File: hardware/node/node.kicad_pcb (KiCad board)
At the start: 4 copper layers, 50 x 50 mm, 71 parts, among them J1 BOOT0_Jumper, J2 FTDI, J3 SMA Female, J4 2 x AA, J5 SWD, Q1 Si2323DDS, SW1 TVCM04N016BB, U1 RFM69HW, U2 SHTC3, U3 AT25DF512C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

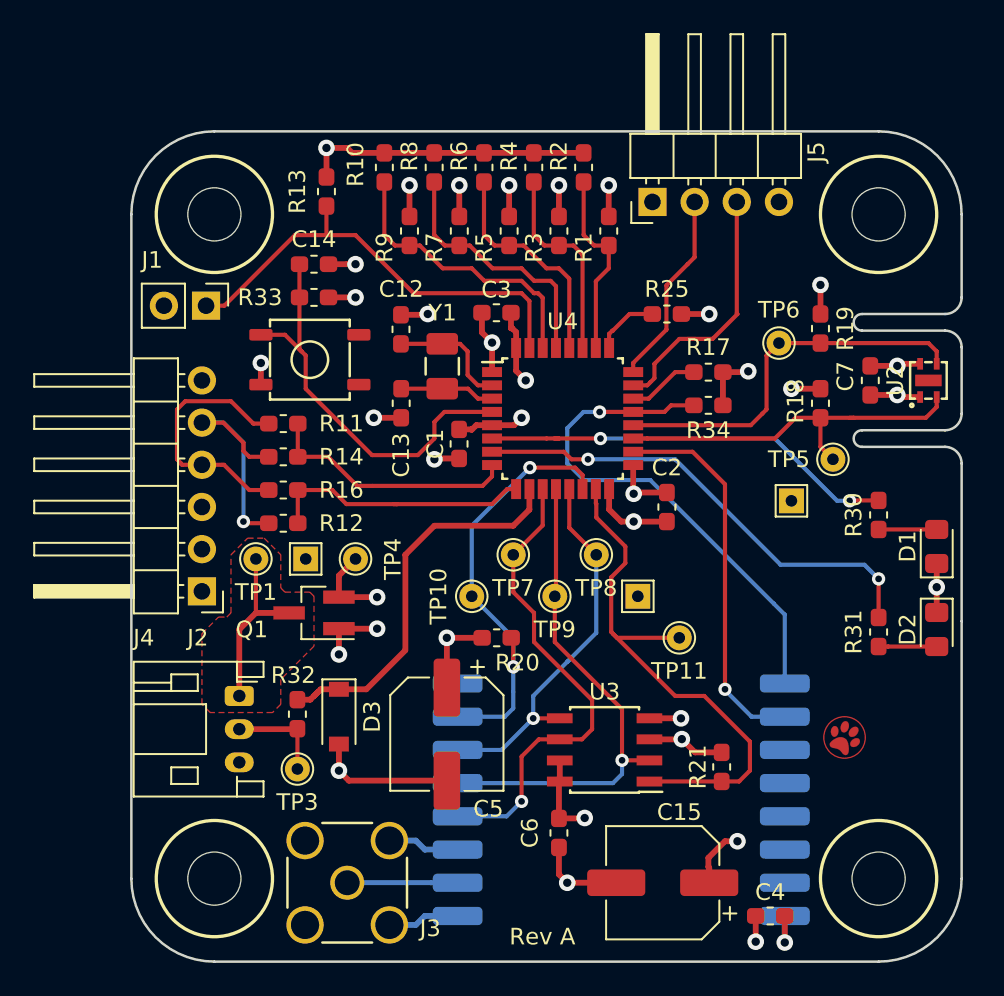
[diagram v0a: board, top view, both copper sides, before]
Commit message: Moved mounting holes. Slightly narrower PCB
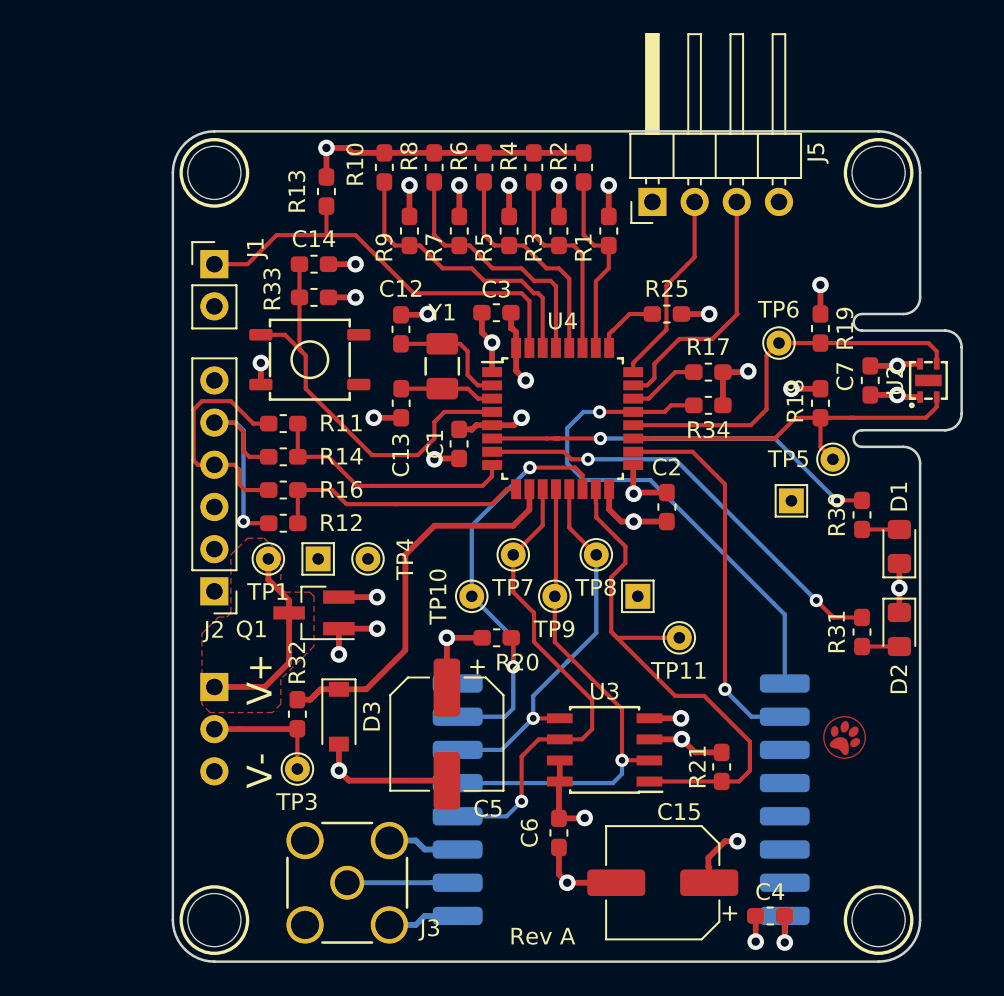
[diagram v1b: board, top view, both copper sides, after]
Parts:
- J2: footprint Connector_PinHeader_2.54mm:PinHeader_1x06_P2.54mm_Horizontal -> Connector_PinHeader_2.54mm:PinHeader_1x06_P2.54mm_Vertical
- J4: footprint Connector_JST:JST_PH_S3B-PH-K_1x03_P2.00mm_Horizontal -> Connector_PinHeader_2.54mm:PinHeader_1x03_P2.54mm_Vertical; moved to B.Cu
- moved J1 2.55 mm to (60.0, 58.0), turned to 0 degrees
- moved H1 2.50 mm to (100.0, 97.5)
- moved H2 2.50 mm to (60.0, 97.5)
- moved H3 2.50 mm to (60.0, 52.5)
- moved H4 2.50 mm to (100.0, 52.5)
- moved D1 2.25 mm to (101.2, 75.0)
- moved D2 2.25 mm to (101.2, 80.0)
- moved J4 1.59 mm to (60.0, 83.5), turned to 180 degrees
- moved R30 1.00 mm to (99.0, 73.1)
- moved R31 1.00 mm to (99.0, 80.2)
- moved J2 0.75 mm to (60.0, 77.7)
- moved TP1 0.75 mm to (63.2, 75.8)
- moved TP2 0.75 mm to (66.2, 75.8)
- moved TP4 0.75 mm to (69.2, 75.8)
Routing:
- net GND: track 288.3 -> 273.5 mm
- net VCC: track 211.7 -> 208.2 mm
- net /LEDG: track 28.8 -> 26.4 mm
- net /BOOT0: track 27.5 -> 25.9 mm
- net /V_BAT_MID: track 5.94 -> 7.44 mm
- net /FTDI_TX: track 15.6 -> 14.3 mm
- net Net-(D2-Pad2): track 3.50 -> 2.25 mm
- net Net-(D1-Pad2): track 3.50 -> 2.25 mm
- net /V_BAT: track 10.7 -> 11.9 mm
- net /LEDR: track 25.1 -> 24.1 mm
- net /FTDI_RX: track 14.5 -> 13.8 mm
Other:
- board size 50 x 50 mm -> 47.5 x 50 mm
- board text added: "Olof Ohlsson Sax 2019-06-03"
- board text removed: "Olof Ohlsson Sax 2019-05-28"

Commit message: Move power connector to other side
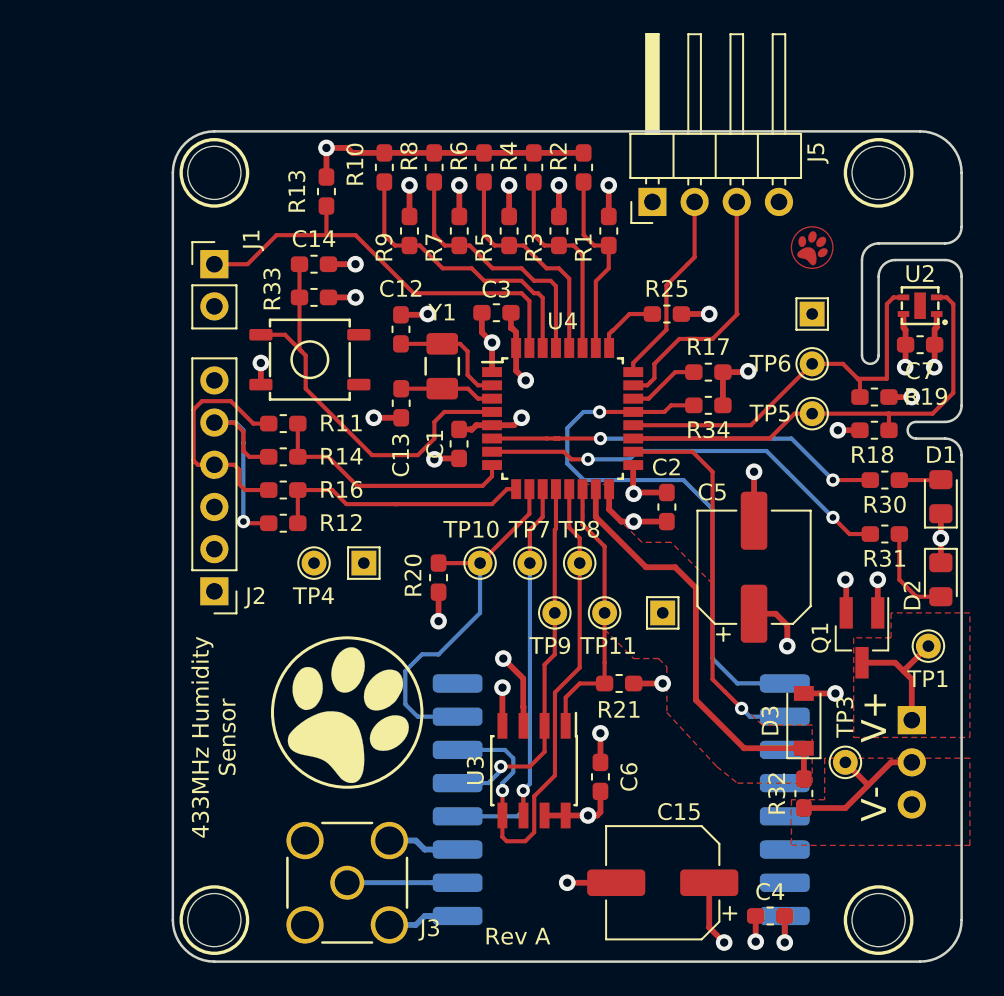
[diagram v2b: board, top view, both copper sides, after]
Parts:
- added G***: LOGO, humidity:paw-large-screen-circ, F.Cu at (68.0, 85.0)
- moved J4 42.0 mm to (102.0, 85.5)
- moved TP1 40.1 mm to (103.0, 81.0)
- moved Q1 33.0 mm to (99.0, 80.5), turned to 270 degrees
- moved TP3 33.0 mm to (98.0, 88.0)
- moved R32 30.9 mm to (95.5, 89.9)
- moved G*** 29.6 mm to (96.0, 57.0)
- moved D3 28.0 mm to (95.5, 85.5), turned to 90 degrees
- moved C5 21.1 mm to (92.5, 76.2), turned to 90 degrees
- moved TP13 11.3 mm to (96.0, 61.0)
- moved R21 7.96 mm to (84.4, 83.2), turned to 0 degrees
- moved R31 6.06 mm to (100.4, 74.2), turned to 180 degrees
- moved R19 5.25 mm to (99.8, 66.0), turned to 0 degrees
- moved R20 5.04 mm to (73.5, 76.9), turned to 270 degrees
- moved TP11 4.74 mm to (83.5, 79.0)
- moved U2 4.53 mm to (102.5, 60.5), turned to 180 degrees
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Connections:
- U4 pad 10: /BAT_MID -> /CS_RFM69
- U4 pad 14: /CS_RFM69 -> /CS_FLASH
- U4 pad 15: /CS_FLASH -> /BAT_MID
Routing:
- net GND: track 273.5 -> 70.1 mm, vias 18 -> 19
- net VCC: track 208.2 -> 54.2 mm, vias 18 -> 20
- net /CS_FLASH: track 33.0 -> 16.7 mm
- net /SPI1_MOSI: track 23.2 -> 32.9 mm
- net /SPI1_MISO: track 30.6 -> 22.3 mm
- net /I2C1_SCL: track 22.7 -> 27.9 mm
- net /CS_RFM69: track 26.6 -> 22.6 mm, vias 2 -> 0
- net /V_BAT: track 11.9 -> 8.00 mm
- net /SPI1_SCK: track 29.0 -> 25.4 mm
- net Net-(D2-Pad2): track 2.25 -> 5.67 mm
- net /RFM69_RST: track 31.3 -> 34.2 mm
- net /V_BAT_MID: track 7.44 -> 9.60 mm
- net /BAT_MID: track 23.9 -> 25.8 mm
- net /LEDG: track 26.4 -> 25.2 mm
- net /I2C1_SDA: track 23.4 -> 24.0 mm
- added copper zone on F.Cu, net /BAT_MID
- added copper zone on F.Cu, net /V_BAT_MID
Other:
- outline, holes or cut-outs redrawn
- board text added: "2019-06-03"

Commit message: Adjust mounting holes
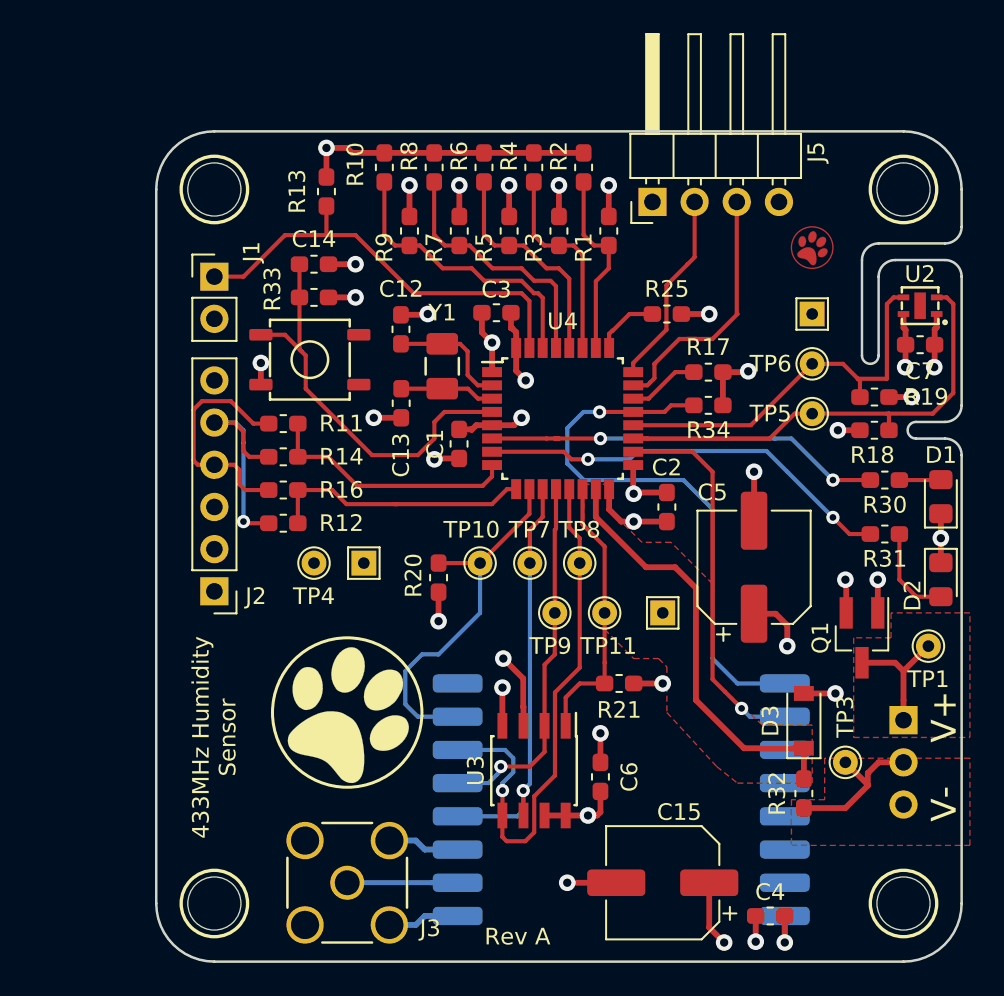
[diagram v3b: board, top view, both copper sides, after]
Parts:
- moved H1 1.80 mm to (101.5, 96.5)
- moved H4 1.80 mm to (101.5, 53.5)
- moved H2 1.00 mm to (60.0, 96.5)
- moved H3 1.00 mm to (60.0, 53.5)
- moved J1 0.75 mm to (60.0, 58.8)
- moved J4 0.50 mm to (101.5, 85.5)
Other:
- board size 47.5 x 50 mm -> 48.5 x 50 mm

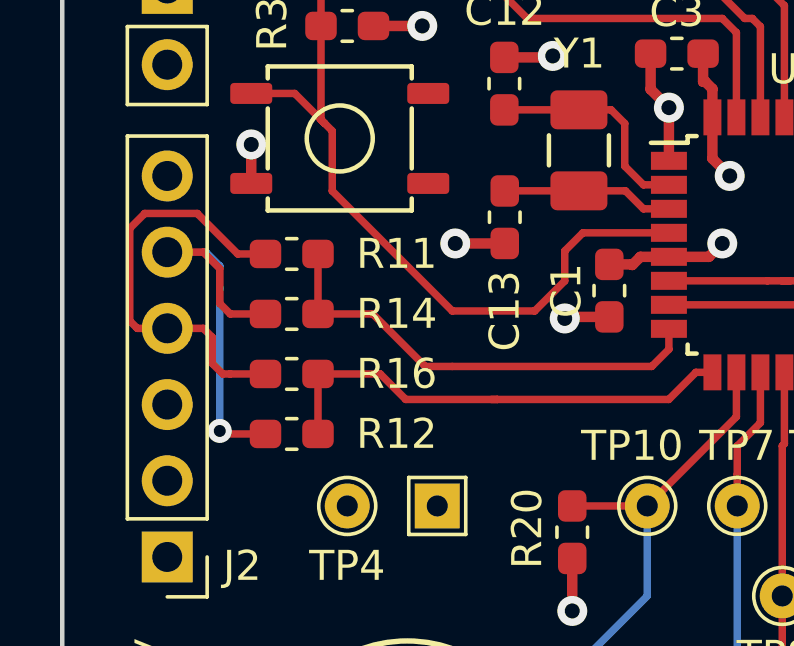
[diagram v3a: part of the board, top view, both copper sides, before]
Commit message: Add resistors as DNP
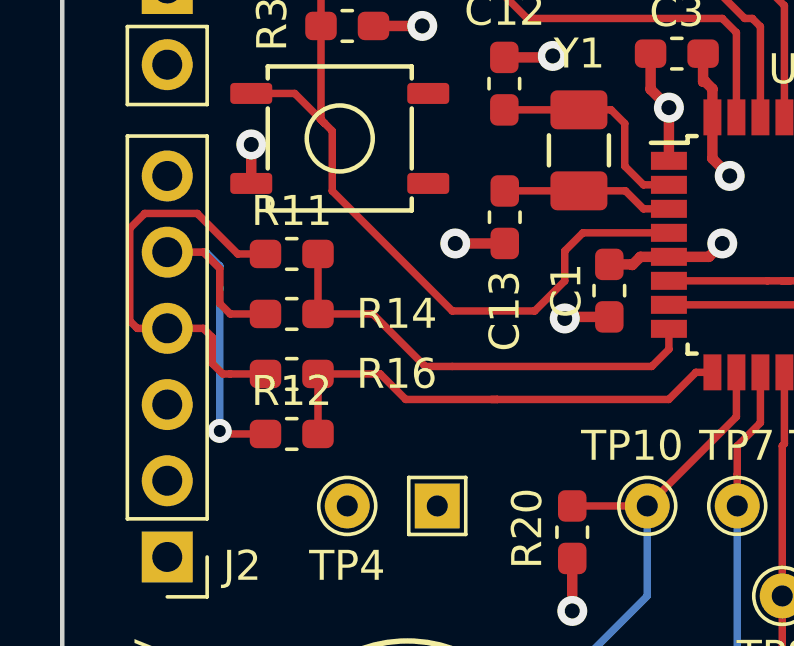
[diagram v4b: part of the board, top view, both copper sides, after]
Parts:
- R11, R12: value 330 -> DNP; footprint Resistor_SMD:R_0603_1608Metric_Pad1.05x0.95mm_HandSolder -> humidity:R_0603_1608Metric_Pad1.05x0.95mm_HandSolder-DNP
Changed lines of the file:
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@@
     (37 F.SilkS user)
     (38 B.Mask user)
-    (39 F.Mask user hide)
+    (39 F.Mask user)
     (40 Dwgs.User user)
     (41 Cmts.User user)
@@
     (add_net VCC)
   )
+  (module humidity:R_0603_1608Metric_Pad1.05x0.95mm_HandSolder-DNP (layer F.Cu)
+    (at 64.15 67.6)
+    (descr "Resistor SMD 0603 (1608 Metric), square (rectangular) end terminal, IPC_7351 nominal with elongated pad for handsoldering. (Body size source: http://www.tortai-tech.com/upload/download/2011102023233369053.pdf), generated with kicad-footprint-generator")
+    (tags "resistor handsolder")
+    (attr smd)
+    (fp_text reference R11 (at 0 -1.43) (layer F.SilkS)
+      (effects (font (size 1 1) (thickness 0.15)))
+    )
+    (fp_text value DNP (at 0 1.43) (layer F.Fab)
+      (effects (font (size 1 1) (thickness 0.15)))
+    )
+    (fp_text user %R (at 0 0) (layer F.Fab)
+      (effects (font (size 0.4 0.4) (thickness 0.06)))
+    )
+    (fp_line (start 1.65 0.73) (end -1.65 0.73) (layer F.CrtYd) (width 0.05))
+    (fp_line (start 1.65 -0.73) (end 1.65 0.73) (layer F.CrtYd) (width 0.05))
+    (fp_line (start -1.65 -0.73) (end 1.65 -0.73) (layer F.CrtYd) (width 0.05))
+    (fp_line (start -1.65 0.73) (end -1.65 -0.73) (layer F.CrtYd) (width 0.05))
+    (fp_line (start -0.171267 0.51) (end 0.171267 0.51) (layer F.SilkS) (width 0.12))
+    (fp_line (start -0.171267 -0.51) (end 0.171267 -0.51) (layer F.SilkS) (width 0.12))
+    (fp_line (start 0.8 0.4) (end -0.8 0.4) (layer F.Fab) (width 0.1))
+    (fp_line (start 0.8 -0.4) (end 0.8 0.4) (layer F.Fab) (width 0.1))
+    (fp_line (start -0.8 -0.4) (end 0.8 -0.4) (layer F.Fab) (width 0.1))
+    (fp_line (start -0.8 0.4) (end -0.8 -0.4) (layer F.Fab) (width 0.1))
+    (pad 2 smd roundrect (at 0.875 0) (size 1.05 0.95) (layers F.Cu F.Mask) (roundrect_rratio 0.25)
+      (net 26 /USART2_TX))
+    (pad 1 smd roundrect (at -0.875 0) (size 1.05 0.95) (layers F.Cu F.Mask) (roundrect_rratio 0.25)
+      (net 41 /FTDI_TX))
+  )
+  (module humidity:R_0603_1608Metric_Pad1.05x0.95mm_HandSolder-DNP (layer F.Cu)
+    (at 64.15 73.6)
+    (descr "Resistor SMD 0603 (1608 Metric), square (rectangular) end terminal, IPC_7351 nominal with elongated pad for handsoldering. (Body size source: http://www.tortai-tech.com/upload/download/2011102023233369053.pdf), generated with kicad-footprint-generator")
+    (tags "resistor handsolder")
+    (attr smd)
+    (fp_text reference R12 (at 0 -1.43) (layer F.SilkS)
+      (effects (font (size 1 1) (thickness 0.15)))
+    )
+    (fp_text value DNP (at 0 1.43) (layer F.Fab)
+      (effects (font (size 1 1) (thickness 0.15)))
+    )
+    (fp_text user %R (at 0 0) (layer F.Fab)
+      (effects (font (size 0.4 0.4) (thickness 0.06)))
+    )
+    (fp_line (start 1.65 0.73) (end -1.65 0.73) (layer F.CrtYd) (width 0.05))
+    (fp_line (start 1.65 -0.73) (end 1.65 0.73) (layer F.CrtYd) (width 0.05))
+    (fp_line (start -1.65 -0.73) (end 1.65 -0.73) (layer F.CrtYd) (width 0.05))
+    (fp_line (start -1.65 0.73) (end -1.65 -0.73) (layer F.CrtYd) (width 0.05))
+    (fp_line (start -0.171267 0.51) (end 0.171267 0.51) (layer F.SilkS) (width 0.12))
+    (fp_line (start -0.171267 -0.51) (end 0.171267 -0.51) (layer F.SilkS) (width 0.12))
+    (fp_line (start 0.8 0.4) (end -0.8 0.4) (layer F.Fab) (width 0.1))
+    (fp_line (start 0.8 -0.4) (end 0.8 0.4) (layer F.Fab) (width 0.1))
+    (fp_line (start -0.8 -0.4) (end 0.8 -0.4) (layer F.Fab) (width 0.1))
+    (fp_line (start -0.8 0.4) (end -0.8 -0.4) (layer F.Fab) (width 0.1))
+    (pad 2 smd roundrect (at 0.875 0) (size 1.05 0.95) (layers F.Cu F.Mask) (roundrect_rratio 0.25)
+      (net 27 /USART2_RX))
+    (pad 1 smd roundrect (at -0.875 0) (size 1.05 0.95) (layers F.Cu F.Mask) (roundrect_rratio 0.25)
+      (net 42 /FTDI_RX))
+  )
   (module humidity:paw-large-screen-circ (layer F.Cu)
     (at 68 85 330)
@@
   )
   (module Resistor_SMD:R_0603_1608Metric_Pad1.05x0.95mm_HandSolder (layer F.Cu)
-    (at 64.15 73.6)
-    (descr "Resistor SMD 0603 (1608 Metric), square (rectangular) end terminal, IPC_7351 nominal with elongated pad for handsoldering. (Body size source: http://www.tortai-tech.com/upload/download/2011102023233369053.pdf), generated with kicad-footprint-generator")
-    (tags "resistor handsolder")
-    (attr smd)
-    (fp_text reference R12 (at 3.5 0 180) (layer F.SilkS)
-      (effects (font (size 1 1) (thickness 0.15)))
-    )
-    (fp_text value 330 (at 0 1.43) (layer F.Fab)
-      (effects (font (size 1 1) (thickness 0.15)))
-    )
-    (fp_line (start -0.8 0.4) (end -0.8 -0.4) (layer F.Fab) (width 0.1))
-    (fp_line (start -0.8 -0.4) (end 0.8 -0.4) (layer F.Fab) (width 0.1))
-    (fp_line (start 0.8 -0.4) (end 0.8 0.4) (layer F.Fab) (width 0.1))
-    (fp_line (start 0.8 0.4) (end -0.8 0.4) (layer F.Fab) (width 0.1))
-    (fp_line (start -0.171267 -0.51) (end 0.171267 -0.51) (layer F.SilkS) (width 0.12))
-    (fp_line (start -0.171267 0.51) (end 0.171267 0.51) (layer F.SilkS) (width 0.12))
-    (fp_line (start -1.65 0.73) (end -1.65 -0.73) (layer F.CrtYd) (width 0.05))
-    (fp_line (start -1.65 -0.73) (end 1.65 -0.73) (layer F.CrtYd) (width 0.05))
-    (fp_line (start 1.65 -0.73) (end 1.65 0.73) (layer F.CrtYd) (width 0.05))
-    (fp_line (start 1.65 0.73) (end -1.65 0.73) (layer F.CrtYd) (width 0.05))
-    (fp_text user %R (at 0 0) (layer F.Fab)
-      (effects (font (size 0.4 0.4) (thickness 0.06)))
-    )
-    (pad 1 smd roundrect (at -0.875 0) (size 1.05 0.95) (layers F.Cu F.Paste F.Mask) (roundrect_rratio 0.25)
-      (net 42 /FTDI_RX))
-    (pad 2 smd roundrect (at 0.875 0) (size 1.05 0.95) (layers F.Cu F.Paste F.Mask) (roundrect_rratio 0.25)
-      (net 27 /USART2_RX))
-    (model ${KISYS3DMOD}/Resistor_SMD.3dshapes/R_0603_1608Metric.wrl
-      (at (xyz 0 0 0))
-      (scale (xyz 1 1 1))
-      (rotate (xyz 0 0 0))
-    )
-  )
-  (module Resistor_SMD:R_0603_1608Metric_Pad1.05x0.95mm_HandSolder (layer F.Cu)
     (at 64.15 71.6)
     (descr "Resistor SMD 0603 (1608 Metric), square (rectangular) end terminal, IPC_7351 nominal with elongated pad for handsoldering. (Body size source: http://www.tortai-tech.com/upload/download/2011102023233369053.pdf), generated with kicad-footprint-generator")
@@
     (model ${KISYS3DMOD}/Resistor_SMD.3dshapes/R_0603_1608Metric.wrl
       (at (xyz 0 0 0))
-      (scale (xyz 1 1 1))
-      (rotate (xyz 0 0 0))
-    )
-  )
-  (module Resistor_SMD:R_0603_1608Metric_Pad1.05x0.95mm_HandSolder (layer F.Cu)
-    (at 64.15 67.6)
-    (descr "Resistor SMD 0603 (1608 Metric), square (rectangular) end terminal, IPC_7351 nominal with elongated pad for handsoldering. (Body size source: http://www.tortai-tech.com/upload/download/2011102023233369053.pdf), generated with kicad-footprint-generator")
-    (tags "resistor handsolder")
-    (attr smd)
-    (fp_text reference R11 (at 3.5 0) (layer F.SilkS)
-      (effects (font (size 1 1) (thickness 0.15)))
-    )
-    (fp_text value 330 (at 0 1.43) (layer F.Fab)
-      (effects (font (size 1 1) (thickness 0.15)))
-    )
-    (fp_text user %R (at 0 0) (layer F.Fab)
-      (effects (font (size 0.4 0.4) (thickness 0.06)))
-    )
-    (fp_line (start 1.65 0.73) (end -1.65 0.73) (layer F.CrtYd) (width 0.05))
-    (fp_line (start 1.65 -0.73) (end 1.65 0.73) (layer F.CrtYd) (width 0.05))
-    (fp_line (start -1.65 -0.73) (end 1.65 -0.73) (layer F.CrtYd) (width 0.05))
-    (fp_line (start -1.65 0.73) (end -1.65 -0.73) (layer F.CrtYd) (width 0.05))
-    (fp_line (start -0.171267 0.51) (end 0.171267 0.51) (layer F.SilkS) (width 0.12))
-    (fp_line (start -0.171267 -0.51) (end 0.171267 -0.51) (layer F.SilkS) (width 0.12))
-    (fp_line (start 0.8 0.4) (end -0.8 0.4) (layer F.Fab) (width 0.1))
-    (fp_line (start 0.8 -0.4) (end 0.8 0.4) (layer F.Fab) (width 0.1))
-    (fp_line (start -0.8 -0.4) (end 0.8 -0.4) (layer F.Fab) (width 0.1))
-    (fp_line (start -0.8 0.4) (end -0.8 -0.4) (layer F.Fab) (width 0.1))
-    (pad 2 smd roundrect (at 0.875 0) (size 1.05 0.95) (layers F.Cu F.Paste F.Mask) (roundrect_rratio 0.25)
-      (net 26 /USART2_TX))
-    (pad 1 smd roundrect (at -0.875 0) (size 1.05 0.95) (layers F.Cu F.Paste F.Mask) (roundrect_rratio 0.25)
-      (net 41 /FTDI_TX))
-    (model ${KISYS3DMOD}/Resistor_SMD.3dshapes/R_0603_1608Metric.wrl
-      (at (xyz 0 0 0))
